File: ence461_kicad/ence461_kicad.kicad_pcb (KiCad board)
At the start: 2 copper layers, 57 parts, among them Q1 Q_PMOS_GSD, U1 LMV324, U2 LMV324, U3 LMV324, U4 74HC3G14DP, U5 LMV321, U6 NCV7344D13R2GOSCT-ND, U7 TPS717DRV-WSON, U8 TPS71433DRVR

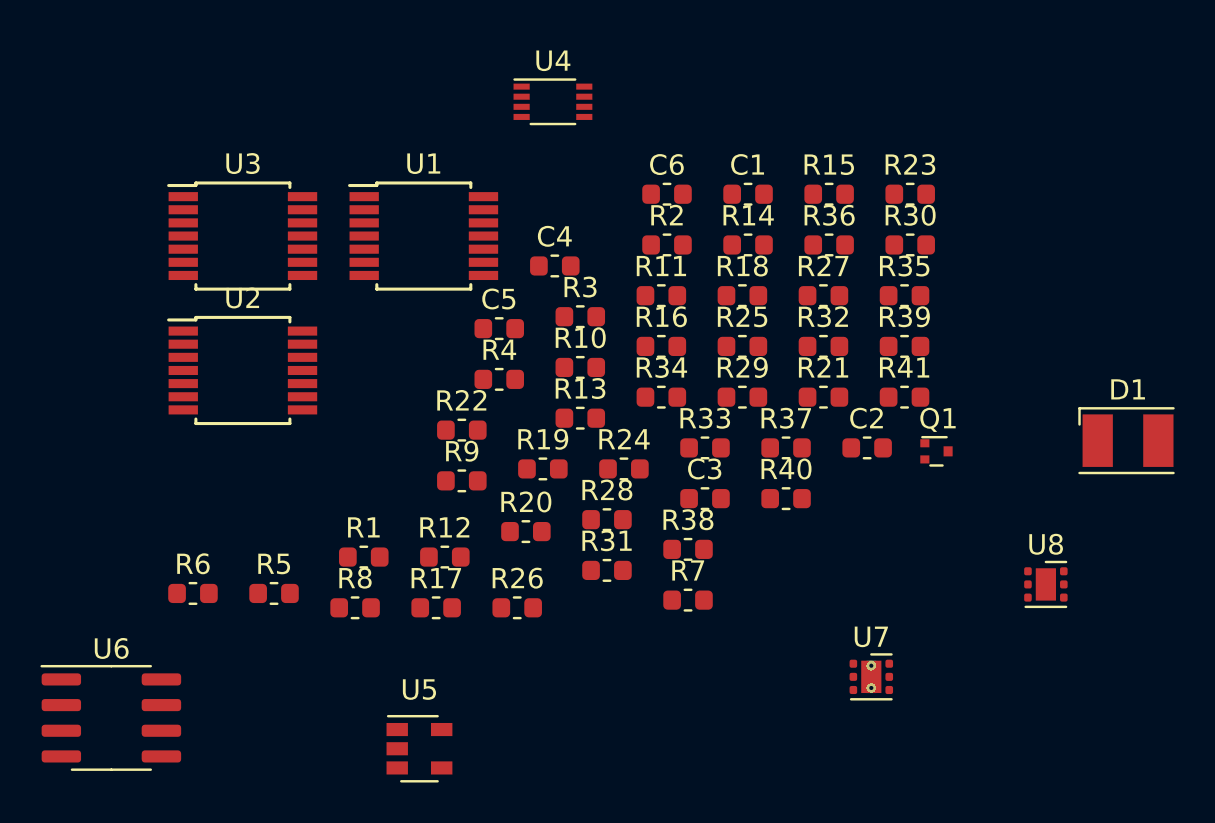
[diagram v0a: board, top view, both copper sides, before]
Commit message: Added micro to schematic. Laid out.
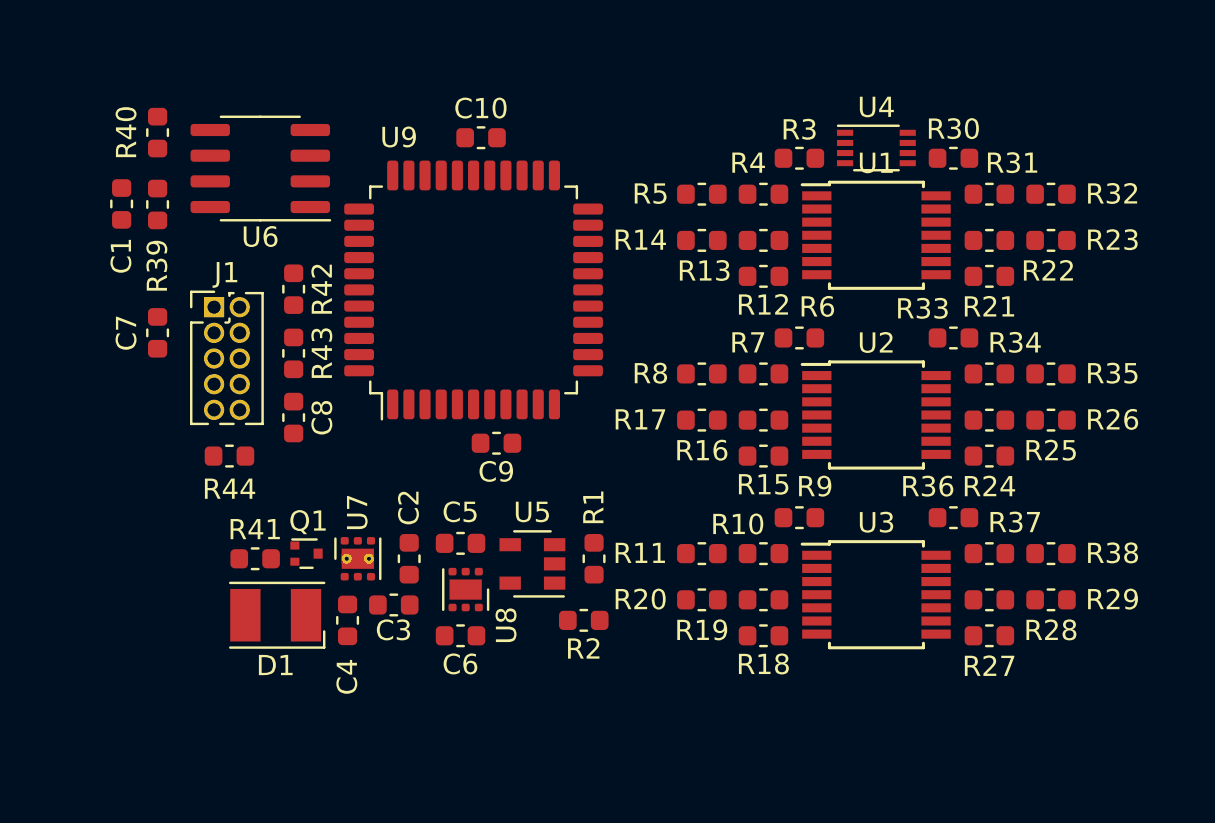
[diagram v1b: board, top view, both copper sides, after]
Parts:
- added C10: 0.1 uF, Capacitor_SMD:C_0603_1608Metric, F.Cu at (126.5, 41.4)
- added C7: 0.1 uF, Capacitor_SMD:C_0603_1608Metric, F.Cu at (110.5, 51.1)
- added C8: 0.1 uF, Capacitor_SMD:C_0603_1608Metric, F.Cu at (117.2, 55.2)
- added C9: 0.1 uF, Capacitor_SMD:C_0603_1608Metric, F.Cu at (127.3, 56.5)
- added J1: Conn_02x05_Odd_Even, Connector_PinHeader_1.27mm:PinHeader_2x05_P1.27mm_Vertical, F.Cu at (113.3, 49.8)
- added R42: 10 K, Resistor_SMD:R_0603_1608Metric, F.Cu at (117.2, 48.9)
- added R43: 10 K, Resistor_SMD:R_0603_1608Metric, F.Cu at (117.2, 52.1)
- added R44: 10 K, Resistor_SMD:R_0603_1608Metric, F.Cu at (114.0, 57.1)
- added U9: MKE16Z32VLD4, Package_QFP:LQFP-44_10x10mm_P0.8mm, F.Cu at (126.1, 48.9)
- moved D1 43.0 mm to (116.3, 65.0), turned to 180 degrees
- moved R39 37.6 mm to (110.5, 44.7), turned to 90 degrees
- moved U3 36.0 mm to (146.1, 64.0)
- moved R40 36.0 mm to (110.5, 41.1), turned to 90 degrees
- moved R41 33.1 mm to (115.3, 62.2)
- moved R6 32.6 mm to (142.2, 51.3), turned to 180 degrees
- moved Q1 31.6 mm to (117.9, 62.0)
- moved U2 31.4 mm to (146.1, 55.1)
- moved C1 31.0 mm to (108.7, 44.7), turned to 90 degrees
- moved R5 28.9 mm to (137.4, 44.2)
- moved U8 28.7 mm to (125.7, 63.8), turned to 270 degrees
- moved U6 28.2 mm to (115.6, 42.9), turned to 180 degrees
- moved R26 28.0 mm to (154.7, 55.4), turned to 180 degrees
- moved R22 27.7 mm to (151.6, 46.5), turned to 180 degrees
- moved R31 26.5 mm to (151.6, 44.2), turned to 180 degrees
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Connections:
- Q1 pad 1: (no net) -> /LED_STATUS
- R12 pad 1: /ADC_02 -> /ADC_01
- R15 pad 1: /ADC_06 -> /ADC_05
- R18 pad 1: /ADC_10 -> /ADC_09
- R21 pad 1: /ADC_03 -> /ADC_02
- R24 pad 1: /ADC_07 -> /ADC_06
- R27 pad 1: /ADC_11 -> /ADC_10
- R3 pad 1: /ADC_01 -> /ADC_00
- R30 pad 1: /ADC_04 -> /ADC_03
- R33 pad 1: /ADC_08 -> /ADC_07
- R36 pad 1: /ADC_12 -> /ADC_11
- R6 pad 1: /ADC_05 -> /ADC_04
- R9 pad 1: /ADC_09 -> /ADC_08
- U1 pad 1: /ADC_01 -> /ADC_00
- U1 pad 14: /ADC_04 -> /ADC_03
- U1 pad 4: /SUPPLY_01 -> /SUPPLY_00
- U1 pad 7: /ADC_02 -> /ADC_01
- U1 pad 8: /ADC_03 -> /ADC_02
- U2 pad 1: /ADC_05 -> /ADC_04
- U2 pad 14: /ADC_08 -> /ADC_07
- U2 pad 4: /SUPPLY_02 -> /SUPPLY_01
- U2 pad 7: /ADC_06 -> /ADC_05
- U2 pad 8: /ADC_07 -> /ADC_06
- U3 pad 1: /ADC_09 -> /ADC_08
- U3 pad 14: /ADC_12 -> /ADC_11
- U3 pad 4: /SUPPLY_03 -> /SUPPLY_02
- U3 pad 7: /ADC_10 -> /ADC_09
- U3 pad 8: /ADC_11 -> /ADC_10
- U4 pad 1: (no net) -> /ENABLE_00
- U4 pad 2: /SUPPLY_03 -> /SUPPLY_02
- U4 pad 3: (no net) -> /ENABLE_01
- U4 pad 5: /SUPPLY_02 -> /SUPPLY_01
- U4 pad 6: (no net) -> /ENABLE_02
- U4 pad 7: /SUPPLY_01 -> /SUPPLY_00
- U6 pad 1: (no net) -> /CAN_TX
- U6 pad 4: (no net) -> /CAN_RX
- U6 pad 5: +3V3 -> +5V
- U6 pad 8: (no net) -> /CAN_STANDBY
- U7 pad 4: (no net) -> /5V_ENABLE

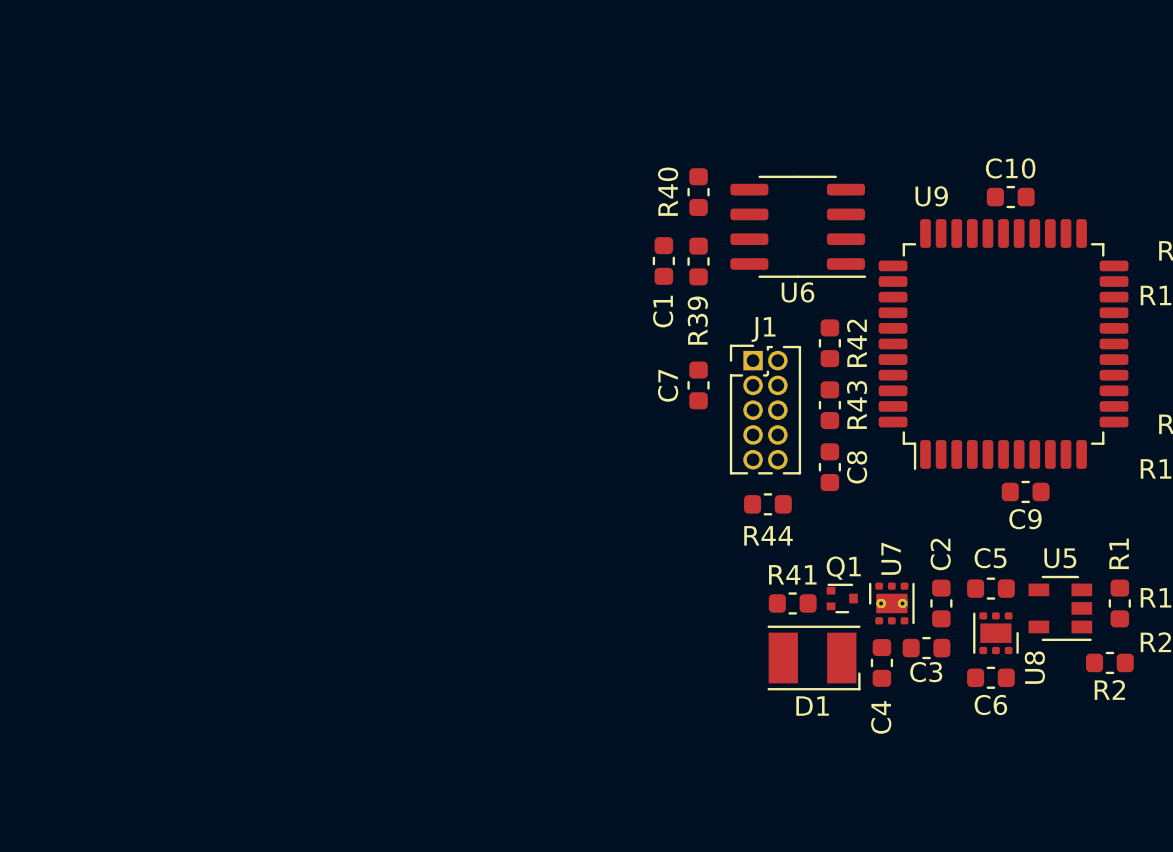
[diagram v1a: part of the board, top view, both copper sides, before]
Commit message: Added symbol for new power supply to schematic.
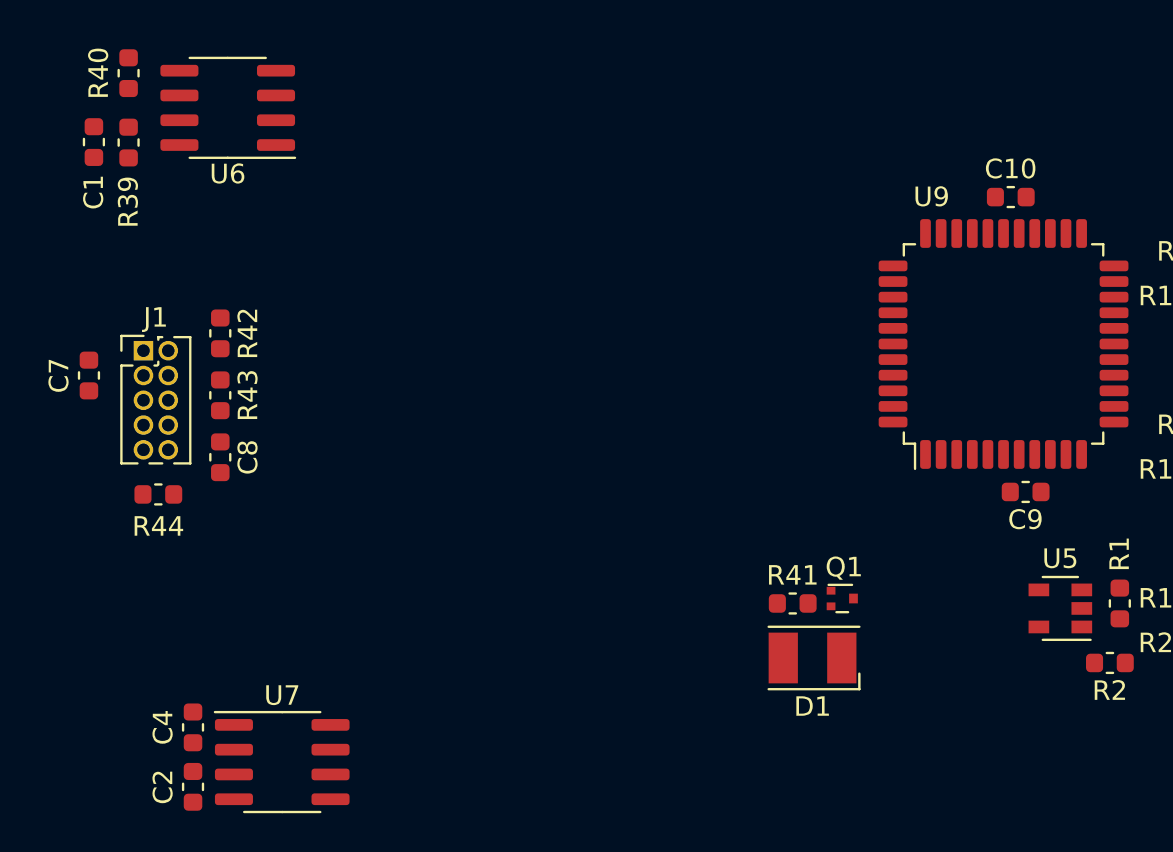
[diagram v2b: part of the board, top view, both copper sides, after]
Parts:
- removed C3: 0.01 uF, Capacitor_SMD:C_0603_1608Metric
- removed C5, C6: 0.47 uF, Capacitor_SMD:C_0603_1608Metric
- removed U8: TPS71433DRVR, Package_SON:WSON-6-1EP_2x2mm_P0.65mm_EP1x1.6mm
- U7: value TPS717DRV-WSON -> MIC5202; footprint Package_SON:WSON-6-1EP_2x2mm_P0.65mm_EP1x1.6mm_ThermalVias -> Package_SO:SOIC-8_3.9x4.9mm_P1.27mm
- moved C2 39.5 mm to (84.6, 71.6)
- moved C4 35.5 mm to (84.6, 68.6)
- moved U7 32.3 mm to (89.2, 70.4), turned to 0 degrees
- moved C8 31.2 mm to (86.0, 54.7)
- moved J1 31.2 mm to (82.0, 49.3)
- moved R42 31.2 mm to (86.0, 48.4)
- moved R43 31.2 mm to (86.0, 51.6)
- moved R44 31.2 mm to (82.8, 56.6)
- moved C7 31.2 mm to (79.2, 50.5)
- moved C1 29.8 mm to (79.5, 38.6)
- moved R39 29.8 mm to (81.3, 38.6)
- moved R40 29.8 mm to (81.3, 35.1)
- moved U6 29.8 mm to (86.4, 36.8)
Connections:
- C10 pad 1: +5V -> /VCC_MICRO
- C2 pad 1: +6V -> /VCC_OPAMP
- C4 pad 1: +5V -> /VCC_MICRO
- C7 pad 1: +5V -> /VCC_MICRO
- C9 pad 2: +5V -> /VCC_MICRO
- J1 pad 1: +5V -> /VCC_MICRO
- R1 pad 1: +5V -> /VCC_OPAMP
- R42 pad 1: +5V -> /VCC_MICRO
- R44 pad 1: +5V -> /VCC_MICRO
- U4 pad 8: +5V -> /VCC_OPAMP
- U5 pad 2: +5V -> /VCC_OPAMP
- U6 pad 3: +5V -> /VCC_MICRO
- U6 pad 5: +5V -> /VCC_MICRO
- U7 pad 1: +5V -> /VCC_MICRO
- U7 pad 2: Net-(C3-Pad1) -> GND
- U7 pad 3: GND -> /VCC_OPAMP
- U7 pad 4: /5V_ENABLE -> GND
- U7 pad 5: (no net) -> /OPAMP_EN
- U7 pad 7: (no net) -> +6V
- U9 pad 13: /5V_ENABLE -> /OPAMP_EN
- U9 pad 28: +5V -> /VCC_MICRO
- U9 pad 5: +5V -> /VCC_MICRO
- U9 pad 6: +5V -> /VCC_MICRO
- U9 pad 7: +5V -> /VCC_MICRO

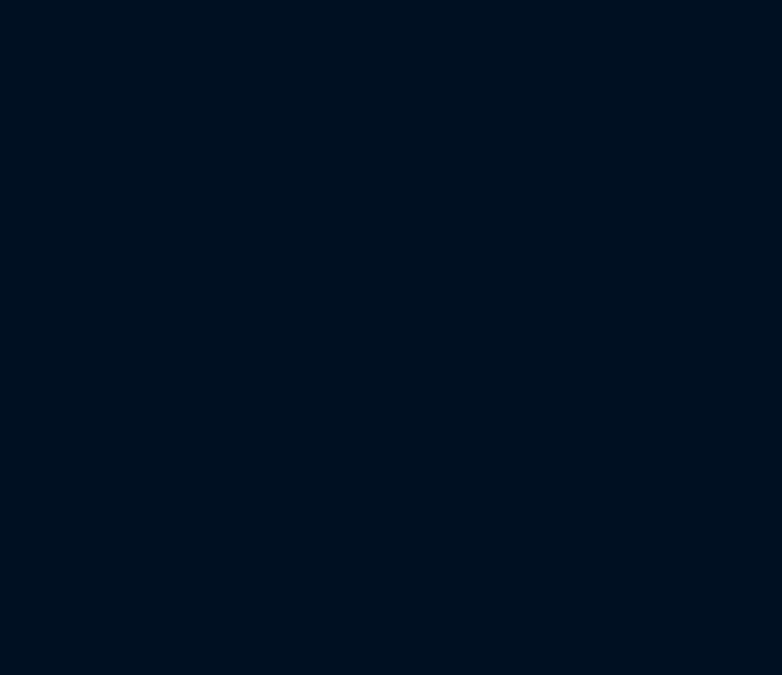
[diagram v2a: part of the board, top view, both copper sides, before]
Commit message: Added RC filtering.
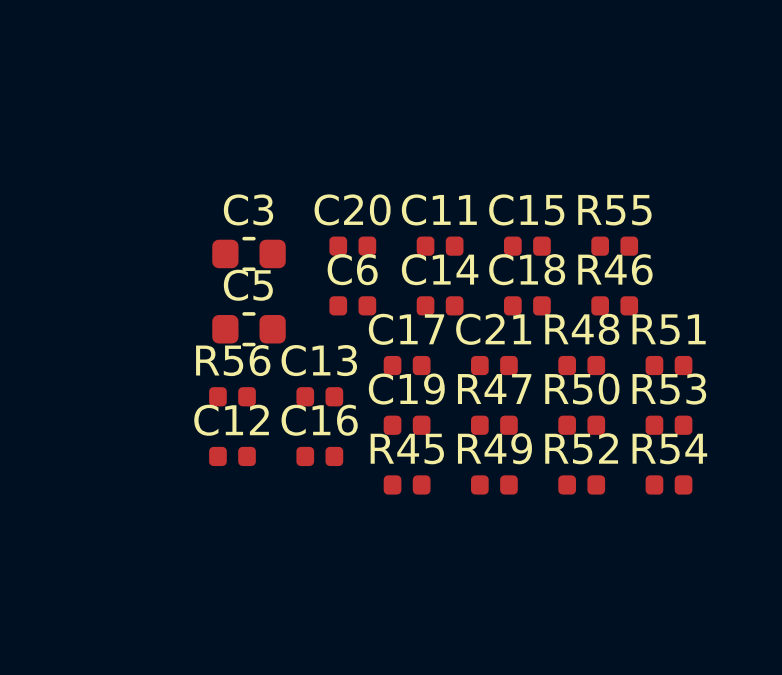
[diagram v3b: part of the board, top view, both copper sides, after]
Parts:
- added C11: 0.47 uF, Capacitor_SMD:C_0402_1005Metric, F.Cu at (183.4, 54.9)
- added C12: 0.47 uF, Capacitor_SMD:C_0402_1005Metric, F.Cu at (176.5, 61.9)
- added C13: 0.47 uF, Capacitor_SMD:C_0402_1005Metric, F.Cu at (179.4, 59.9)
- added C14: 0.47 uF, Capacitor_SMD:C_0402_1005Metric, F.Cu at (183.4, 56.8)
- added C15: 0.47 uF, Capacitor_SMD:C_0402_1005Metric, F.Cu at (186.3, 54.9)
- added C16: 0.47 uF, Capacitor_SMD:C_0402_1005Metric, F.Cu at (179.4, 61.9)
- added C17: 0.47 uF, Capacitor_SMD:C_0402_1005Metric, F.Cu at (182.3, 58.8)
- added C18: 0.47 uF, Capacitor_SMD:C_0402_1005Metric, F.Cu at (186.3, 56.8)
- added C19: 0.47 uF, Capacitor_SMD:C_0402_1005Metric, F.Cu at (182.3, 60.8)
- added C20: 0.47 uF, Capacitor_SMD:C_0402_1005Metric, F.Cu at (180.5, 54.9)
- added C21: 0.47 uF, Capacitor_SMD:C_0402_1005Metric, F.Cu at (185.2, 58.8)
- added C3: 1 nF, Capacitor_SMD:C_0603_1608Metric, F.Cu at (177.0, 55.1)
- added C5: 100 nF, Capacitor_SMD:C_0603_1608Metric, F.Cu at (177.0, 57.6)
- added C6: 0.47 uF, Capacitor_SMD:C_0402_1005Metric, F.Cu at (180.5, 56.8)
- added R45: 560 R, Resistor_SMD:R_0402_1005Metric, F.Cu at (182.3, 62.8)
- added R46: 560 R, Resistor_SMD:R_0402_1005Metric, F.Cu at (189.2, 56.8)
- added R47: 560 R, Resistor_SMD:R_0402_1005Metric, F.Cu at (185.2, 60.8)
- added R48: 560 R, Resistor_SMD:R_0402_1005Metric, F.Cu at (188.1, 58.8)
- added R49: 560 R, Resistor_SMD:R_0402_1005Metric, F.Cu at (185.2, 62.8)
- added R50: 560 R, Resistor_SMD:R_0402_1005Metric, F.Cu at (188.1, 60.8)
- added R51: 560 R, Resistor_SMD:R_0402_1005Metric, F.Cu at (191.0, 58.8)
- added R52: 560 R, Resistor_SMD:R_0402_1005Metric, F.Cu at (188.1, 62.8)
- added R53: 560 R, Resistor_SMD:R_0402_1005Metric, F.Cu at (191.0, 60.8)
- added R54: 560 R, Resistor_SMD:R_0402_1005Metric, F.Cu at (191.0, 62.8)
- added R55: 560 R, Resistor_SMD:R_0402_1005Metric, F.Cu at (189.2, 54.9)
- added R56: 560 R, Resistor_SMD:R_0402_1005Metric, F.Cu at (176.5, 59.9)
- C9: value 0.1 uF -> 1 uF
- R10, R13, R16, R19, R22, R25, R28, R31, R34, R37, R4, R7: value 1 K -> 920 R
- R11, R14, R17, R20, R23, R26, R29, R32, R35, R38, R5, R8: value 10 R -> 8.2 R
- R12, R15, R18, R21, R24, R27, R3, R30, R33, R36, R6, R9: value 100 K -> 130 K
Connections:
- C9 pad 1: GND -> /VCC_MICRO
- C9 pad 2: /VCC_MICRO -> GND
- R12 pad 1: /ADC_01 -> /FILTER_01
- R15 pad 1: /ADC_05 -> /FILTER_05
- R18 pad 1: /ADC_09 -> /FILTER_09
- R21 pad 1: /ADC_02 -> /FILTER_02
- R24 pad 1: /ADC_06 -> /FILTER_06
- R27 pad 1: /ADC_10 -> /FILTER_10
- R3 pad 1: /ADC_00 -> /FILTER_00
- R30 pad 1: /ADC_03 -> /FILTER_03
- R33 pad 1: /ADC_07 -> /FILTER_07
- R36 pad 1: /ADC_11 -> /FILTER_11
- R6 pad 1: /ADC_04 -> /FILTER_04
- R9 pad 1: /ADC_08 -> /FILTER_08
- U1 pad 1: /ADC_00 -> /FILTER_00
- U1 pad 14: /ADC_03 -> /FILTER_03
- U1 pad 7: /ADC_01 -> /FILTER_01
- U1 pad 8: /ADC_02 -> /FILTER_02
- U2 pad 1: /ADC_04 -> /FILTER_04
- U2 pad 14: /ADC_07 -> /FILTER_07
- U2 pad 7: /ADC_05 -> /FILTER_05
- U2 pad 8: /ADC_06 -> /FILTER_06
- U3 pad 1: /ADC_08 -> /FILTER_08
- U3 pad 14: /ADC_11 -> /FILTER_11
- U3 pad 7: /ADC_09 -> /FILTER_09
- U3 pad 8: /ADC_10 -> /FILTER_10

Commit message: Almost there!
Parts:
- added H1: MountingHole, MountingHole:MountingHole_3mm, F.Cu at (136.9, 41.4)
- added H2: MountingHole, MountingHole:MountingHole_3mm, F.Cu at (136.9, 62.2)
- added H3: MountingHole, MountingHole:MountingHole_3mm, F.Cu at (105.4, 62.2)
- added J2: INPUT_0, Connector_PinSocket_1.27mm:PinSocket_1x04_P1.27mm_Vertical, B.Cu at (143.5, 39.9)
- added J3: INPUT_1, Connector_PinSocket_1.27mm:PinSocket_1x04_P1.27mm_Vertical, B.Cu at (152.1, 39.9)
- added J4: CANBUS, Connector_PinHeader_1.27mm:PinHeader_2x05_P1.27mm_Vertical, F.Cu at (105.4, 45.3)
- added J5: INPUT_2, Connector_PinSocket_1.27mm:PinSocket_1x04_P1.27mm_Vertical, B.Cu at (147.6, 65.9)
- added JP1: CAN_HIGH, Jumper:SolderJumper-3_P1.3mm_Open_Pad1.0x1.5mm, F.Cu at (109.6, 45.5)
- added JP2: CAN_LOW, Jumper:SolderJumper-3_P1.3mm_Open_Pad1.0x1.5mm, F.Cu at (109.6, 40.6)
- J1: value Conn_02x05_Odd_Even -> SWD
- moved R48 71.5 mm to (117.5, 47.2), turned to 180 degrees
- moved R45 66.2 mm to (117.5, 49.2), turned to 180 degrees
- moved R51 66.2 mm to (127.1, 42.0), turned to 90 degrees
- moved R54 65.4 mm to (129.1, 42.0), turned to 90 degrees
- moved C6 63.3 mm to (117.5, 50.2), turned to 180 degrees
- moved C13 63.0 mm to (117.5, 48.2), turned to 180 degrees
- moved R46 60.0 mm to (131.1, 42.0), turned to 90 degrees
- moved C19 57.4 mm to (128.1, 42.0), turned to 90 degrees
- moved C16 56.9 mm to (126.0, 42.0), turned to 90 degrees
- moved R49 56.1 mm to (133.2, 42.0), turned to 90 degrees
- moved R53 55.9 mm to (135.6, 53.8)
- moved R52 55.3 mm to (135.6, 45.7)
- moved C11 54.8 mm to (130.1, 42.0), turned to 90 degrees
- moved R55 54.1 mm to (135.6, 47.7)
- moved C14 53.4 mm to (132.1, 42.0), turned to 90 degrees
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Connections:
- U1 pad 10: (no net) -> /CURRENT_02
- U1 pad 12: (no net) -> /CURRENT_03
- U1 pad 3: (no net) -> /CURRENT_00
- U1 pad 5: (no net) -> /CURRENT_01
- U2 pad 10: (no net) -> /CURRENT_06
- U2 pad 12: (no net) -> /CURRENT_07
- U2 pad 3: (no net) -> /CURRENT_04
- U2 pad 5: (no net) -> /CURRENT_05
- U3 pad 10: (no net) -> /CURRENT_10
- U3 pad 12: (no net) -> /CURRENT_11
- U3 pad 3: (no net) -> /CURRENT_08
- U3 pad 5: (no net) -> /CURRENT_09
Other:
- board outline added: 58 x 30 mm

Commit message: Finished layout.
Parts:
- added J6: POWER, ence461_kicad:TB002-500, F.Cu at (101.3, 62.7)
- moved C2 19.8 mm to (118.5, 63.2), turned to 90 degrees
- moved R2 18.2 mm to (128.9, 63.0), turned to 0 degrees
- moved U5 16.4 mm to (131.4, 65.8), turned to 0 degrees
- moved C4 15.3 mm to (118.5, 66.3), turned to 90 degrees
- moved U7 13.2 mm to (113.9, 65.0), turned to 180 degrees
- moved R1 12.3 mm to (128.4, 66.0), turned to 90 degrees
- moved R44 11.7 mm to (116.3, 55.6), turned to 90 degrees
- moved H3 7.10 mm to (111.8, 59.1)
- moved C3 3.51 mm to (123.5, 60.5), turned to 270 degrees
- moved C5 1.20 mm to (125.2, 60.5), turned to 270 degrees
- moved C9 1.14 mm to (126.7, 60.5), turned to 270 degrees
